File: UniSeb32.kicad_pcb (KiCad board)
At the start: 2 copper layers, 72 x 100 mm, 35 parts, among them IC1 WEMOS-D1-MINI, IC2 GY-BME280-3.3, IC3 AMS1117-3.3, IC4 MCP23008SS, IC5 RT9400, IC6 AMS5915, J1 22-27-2031-03, X61 JST-XH-05-PIN-LONG-PAD, X7 0446200002

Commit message: .
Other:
- board text added: "UniSeb32 v1.0"
- board text removed: "UniSeb8266 v1.1"

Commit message: .
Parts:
- removed @HOLE0, @HOLE1, @HOLE2, @HOLE3: , 
- removed I2C-1, I2C-2, I2C-3: MA05-1_WON, UniSeb8266:MA05-1_WON
- removed IC1: WEMOS-D1-MINI, UniSeb8266:WEMOS-D1-MINI
- removed IC2: GY-BME280-3.3, UniSeb8266:GY-BME280-3.3
- removed IC6: AMS5915, UniSeb8266:AMS5915
- removed LED1: , UniSeb8266:LED3MM
- removed R3: 390, UniSeb8266:R1206
- removed U$2: HLK-PM01, UniSeb8266:HLK-PM01
- removed the X1 at (130.8, 74.4)
- removed the X2 at (124.6, 139.1)
- removed X7: 0446200002, UniSeb8266:0446200002
- added C10: 100n, Capacitor_SMD:C_0603_1608Metric, B.Cu at (165.8, 96.8)
- added C11: 10n, Capacitor_SMD:C_0603_1608Metric, B.Cu at (179.8, 84.2)
- added C12: 2.2µ, Capacitor_SMD:C_0603_1608Metric, B.Cu at (179.8, 86.0)
- added C13: 100n, Capacitor_SMD:C_0603_1608Metric, B.Cu at (163.8, 96.8)
- added C14: 30p, Capacitor_SMD:C_0603_1608Metric, B.Cu at (171.8, 81.2)
- added C15: 30p, Capacitor_SMD:C_0603_1608Metric, B.Cu at (177.8, 81.2)
- added C3: 22µ, Capacitor_SMD:C_1206_3216Metric, B.Cu at (159.0, 97.0)
- added C4: 100n, Capacitor_SMD:C_0603_1608Metric, B.Cu at (163.5, 67.5)
- added C5: 10p, Capacitor_SMD:C_0603_1608Metric, B.Cu at (169.0, 75.9)
- added C6: 10p, Capacitor_SMD:C_0603_1608Metric, B.Cu at (166.2, 75.9)
- added C7: 10p, Capacitor_SMD:C_0603_1608Metric, B.Cu at (161.5, 67.5)
- added C8: 10p, Capacitor_SMD:C_0603_1608Metric, B.Cu at (159.5, 67.5)
- added C9: 10uf, Capacitor_SMD:C_0603_1608Metric, B.Cu at (164.5, 83.2)
- added J2: ARJM11C7-114-BA-EW2, _custom:ARJM11C7-114-BA-EW2, F.Cu at (162.6, 73.0)
- added J3: Conn_02x05_Odd_Even, Connector_PinHeader_2.54mm:PinHeader_2x05_P2.54mm_Vertical_SMD, F.Cu at (175.5, 89.5)
- added J7: Conn_01x02_Female, TerminalBlock:TerminalBlock_bornier-2_P5.08mm, F.Cu at (128.3, 74.4)
- added J8: Conn_01x02_Female, TerminalBlock:TerminalBlock_bornier-2_P5.08mm, F.Cu at (124.6, 141.7)
- added L1: L, Inductor_SMD:L_0805_2012Metric, B.Cu at (164.5, 93.8)
- added R10: 49.9 %1, Resistor_SMD:R_0603_1608Metric, B.Cu at (164.5, 92.0)
- added R11: 49.9 %1, Resistor_SMD:R_0603_1608Metric, B.Cu at (164.5, 86.8)
- added R12: 2.2k, Resistor_SMD:R_0603_1608Metric, B.Cu at (160.5, 62.0)
- added R13: 49.9 %1, Resistor_SMD:R_0603_1608Metric, B.Cu at (164.5, 88.5)
- added R14: 12.1k, Resistor_SMD:R_0603_1608Metric, B.Cu at (164.5, 85.0)
- added R15: 10k, Resistor_SMD:R_0603_1608Metric, B.Cu at (181.2, 91.2)
- added R16: 10k, Resistor_SMD:R_0603_1608Metric, B.Cu at (173.0, 122.0)
- added R17: 10k, Resistor_SMD:R_0603_1608Metric, B.Cu at (181.2, 94.8)
- added R18: 10k, Resistor_SMD:R_0603_1608Metric, B.Cu at (181.2, 93.0)
- added R19: 10k, Resistor_SMD:R_0603_1608Metric, B.Cu at (181.2, 87.8)
- added R2: 0, Resistor_SMD:R_0603_1608Metric, B.Cu at (162.5, 80.5)
- added R20: 10k, Resistor_SMD:R_0603_1608Metric, B.Cu at (181.2, 89.5)
- added R8: 2.2k, Resistor_SMD:R_0603_1608Metric, B.Cu at (162.5, 62.0)
- added R9: 49.9 %1, Resistor_SMD:R_0603_1608Metric, B.Cu at (164.5, 90.2)
- added U1: mini_esp32, ESP32_mini:ESP32_mini, F.Cu at (169.0, 114.5)
- added U2: LAN8720A, Package_DFN_QFN:QFN-24-1EP_4x4mm_P0.5mm_EP2.6x2.6mm, B.Cu at (173.0, 89.3)
- added U4: AMS5919, _custom:AMS5915, F.Cu at (156.0, 85.0)
- added U5: module_bme280, usini_sensors:module_bme280, F.Cu at (177.9, 67.2)
- added U8: HLK-PM01, Converter_ACDC:Converter_ACDC_HiLink_HLK-PMxx, F.Cu at (135.5, 83.5)
- added Y1: Crystal_GND23, Crystal:Crystal_SMD_3225-4Pin_3.2x2.5mm, B.Cu at (174.8, 81.2)
- C1: value 100µF -> 100µ; footprint UniSeb8266:E2,5-6 -> Capacitor_THT:CP_Radial_D5.0mm_P2.50mm
- C2: value 22µF -> 22µ tantalium; footprint UniSeb8266:E2,5-6 -> Capacitor_THT:CP_Radial_D5.0mm_P2.50mm
- F1: footprint UniSeb8266:TR5 -> Fuse:Fuse_Littelfuse_372_D8.50mm
- F2: value 1A T -> 550mA MT; footprint UniSeb8266:TR5 -> Fuse:Fuse_Littelfuse_372_D8.50mm
- J1: value 22-27-2031-03 -> IO; footprint UniSeb8266:6410-03 -> Connector:FanPinHeader_1x03_P2.54mm_Vertical
- J6: renamed from X61; value JST-XH-05-PIN-LONG-PAD -> SDS011; footprint UniSeb8266:JST-XH-05-PACKAGE-LONG-PAD -> Connector_JST:JST_XH_B5B-XH-A_1x05_P2.50mm_Vertical
- JP1: renamed from SJ1; value (none) -> SolderJumper_2_Open; footprint UniSeb8266:SJ -> Jumper:SolderJumper-2_P1.3mm_Open_Pad1.0x1.5mm
- JP2: renamed from SJ2; value (none) -> SolderJumper_3_Open; footprint UniSeb8266:SJ_2 -> Jumper:SolderJumper-3_P1.3mm_Open_Pad1.0x1.5mm_NumberLabels
- R1: footprint UniSeb8266:P0613V -> Resistor_THT:R_Axial_DIN0414_L11.9mm_D4.5mm_P5.08mm_Vertical
- R4, R5: footprint UniSeb8266:R1206 -> Resistor_SMD:R_0603_1608Metric
- R6, R7: value (none) -> R; footprint UniSeb8266:R1206 -> Resistor_SMD:R_0603_1608Metric
- U3: renamed from IC3; footprint UniSeb8266:SOT223 -> Package_TO_SOT_SMD:SOT-223-3_TabPin2
- U6: renamed from IC5; footprint UniSeb8266:RT9400 -> _custom:RT9400
- U7: renamed from IC4; value MCP23008SS -> MCP23008-xSS; footprint UniSeb8266:SSOP20 -> Package_SO:SSOP-20_5.3x7.2mm_P0.65mm
- X1: renamed from X8; value (none) -> 233-508; footprint UniSeb8266:233-508 -> con-wago:con-wago-233-508
- X2: renamed from X3; value (none) -> 233-503; footprint UniSeb8266:233-503 -> con-wago:con-wago-233-503
- X3: renamed from X5; value (none) -> 233-504; footprint UniSeb8266:233-504 -> con-wago:con-wago-233-504
- moved C1 46.5 mm to (129.5, 126.9), turned to -90 degrees
- moved C2 36.3 mm to (138.0, 127.0), turned to -90 degrees
- moved U6 34.4 mm to (146.0, 82.5)
- moved U3 31.4 mm to (132.0, 105.0), turned to 90 degrees
- moved R5 24.5 mm to (177.5, 122.0)
- moved R7 13.2 mm to (139.0, 103.8)
- moved F2 10.6 mm to (126.5, 118.0)
- moved R4 10.2 mm to (170.0, 122.0), turned to 90 degrees
- moved R1 5.79 mm to (134.5, 123.0), turned to 90 degrees
- moved J6 5.21 mm to (160.0, 129.5), turned to 0 degrees
- moved F1 3.36 mm to (119.0, 68.5)
- moved J1 2.86 mm to (176.0, 139.0), turned to 0 degrees
- moved R6 1.73 mm to (139.0, 108.5), turned to 90 degrees
- turned U7 to 180 degrees
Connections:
- net COUNTER renamed /COUNTER
- net ONEWIRE renamed /ONEWIRE
- J1 pad 2: D5 -> /IO33
- J1 pad 3: D0 -> /IO32
- J6 pad 1: (no net) -> /SDS_TX
- J6 pad 2: +5V -> /SDS_RX
- J6 pad 4: SDS_RX -> +5V
- J6 pad 5: SDS_TX -> unconnected-(J6-Pad5)
- JP1 pad 1: VCC -> +5V
- JP1 pad 2: +5V -> VCC
- JP2 pad 1: N$7 -> Net-(JP2-Pad1)
- R1 pad 1: VCC -> GND
- R1 pad 2: GND -> VCC
- R4 pad 2: +3V3 -> +3.3V
- R5 pad 2: +3V3 -> +3.3V
- R6 pad 2: N$21 -> Net-(R7-Pad1)
- R7 pad 1: N$7 -> Net-(R7-Pad1)
- R7 pad 2: N$21 -> Net-(JP2-Pad1)
- U3 pad 2: +3V3 -> +3.3V
- U6 pad P$1: N$18 -> /VA1
- U6 pad P$2: N$17 -> /VA2
- U6 pad P$3: N$16 -> /VB1
- U6 pad P$4: N$4 -> /VB2
- U6 pad P$6: N$7 -> Net-(JP2-Pad1)
- U6 pad P$7: N$21 -> Net-(R7-Pad1)
- U7 pad 1: SCL -> /SCL
- U7 pad 10: (no net) -> unconnected-(U7-Pad10)
- U7 pad 11: (no net) -> unconnected-(U7-Pad11)
- U7 pad 2: SDA -> /SDA
- U7 pad 20: +3V3 -> +3.3V
- U7 pad 6: +3V3 -> +3.3V
- U7 pad 7: (no net) -> unconnected-(U7-Pad7)
- U7 pad 8: EXP-INT -> unconnected-(U7-Pad8)
- X1 pad A1: (no net) -> unconnected-(X1-PadA1)
- X1 pad A2: (no net) -> unconnected-(X1-PadA2)
- X1 pad A3: (no net) -> unconnected-(X1-PadA3)
- X1 pad A4: (no net) -> unconnected-(X1-PadA4)
- X1 pad A5: (no net) -> unconnected-(X1-PadA5)
- X1 pad A6: (no net) -> unconnected-(X1-PadA6)
- X1 pad A7: (no net) -> unconnected-(X1-PadA7)
- X1 pad A8: (no net) -> unconnected-(X1-PadA8)
- X2 pad A1: (no net) -> unconnected-(X2-PadA1)
- X2 pad A2: (no net) -> unconnected-(X2-PadA2)
- X2 pad A3: (no net) -> unconnected-(X2-PadA3)
- X2 pad B3: +3V3 -> +3.3V
- X3 pad A1: (no net) -> unconnected-(X3-PadA1)
- X3 pad A2: (no net) -> unconnected-(X3-PadA2)
- X3 pad A3: (no net) -> unconnected-(X3-PadA3)
- X3 pad A4: (no net) -> unconnected-(X3-PadA4)
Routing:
- net +3V3: track 165.3 -> 0.00 mm, vias 2 -> 0
- net SCL: track 127.1 -> 0.00 mm, vias 1 -> 0
- net +5V: track 222.2 -> 112.4 mm, vias 3 -> 1
- net SDA: track 109.3 -> 0.00 mm, vias 1 -> 0
- net +3.3V: track 0.00 -> 60.5 mm, vias 0 -> 1
- net /COUNTER: track 55.4 -> 0.00 mm, vias 2 -> 0
- net N$7: track 48.9 -> 0.00 mm, vias 1 -> 0
- net D0: track 46.2 -> 0.00 mm, vias 3 -> 0
- net D5: track 43.9 -> 0.00 mm, vias 2 -> 0
- net N$18: track 38.4 -> 0.00 mm
- net SDS_TX: track 34.9 -> 0.00 mm
- net N$4: track 34.2 -> 0.00 mm
- net VCC: track 34.0 -> 0.00 mm, vias 1 -> 0
- net /ONEWIRE: track 57.2 -> 25.2 mm, vias 2 -> 1
- net /VA1: track 0.00 -> 31.6 mm
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
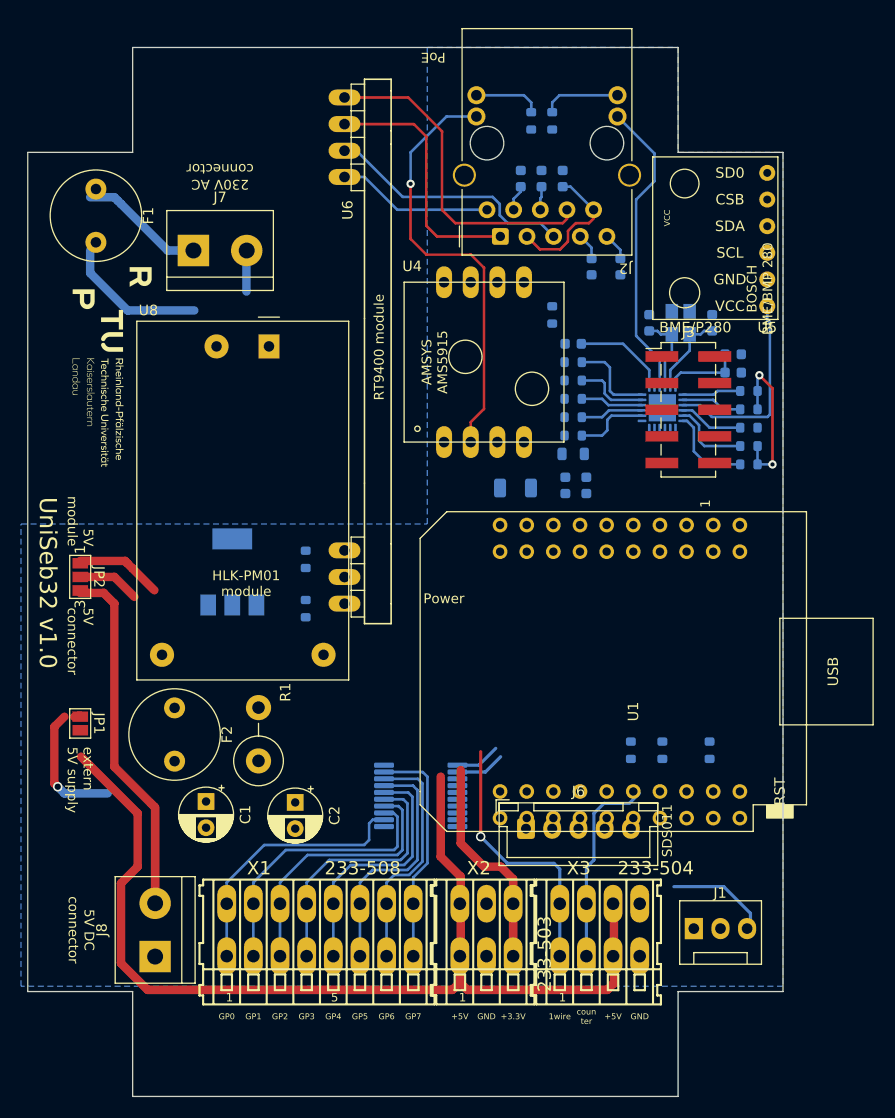
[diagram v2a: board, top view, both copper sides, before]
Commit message: switched to 4 layer PCB. Routed remaining airwires
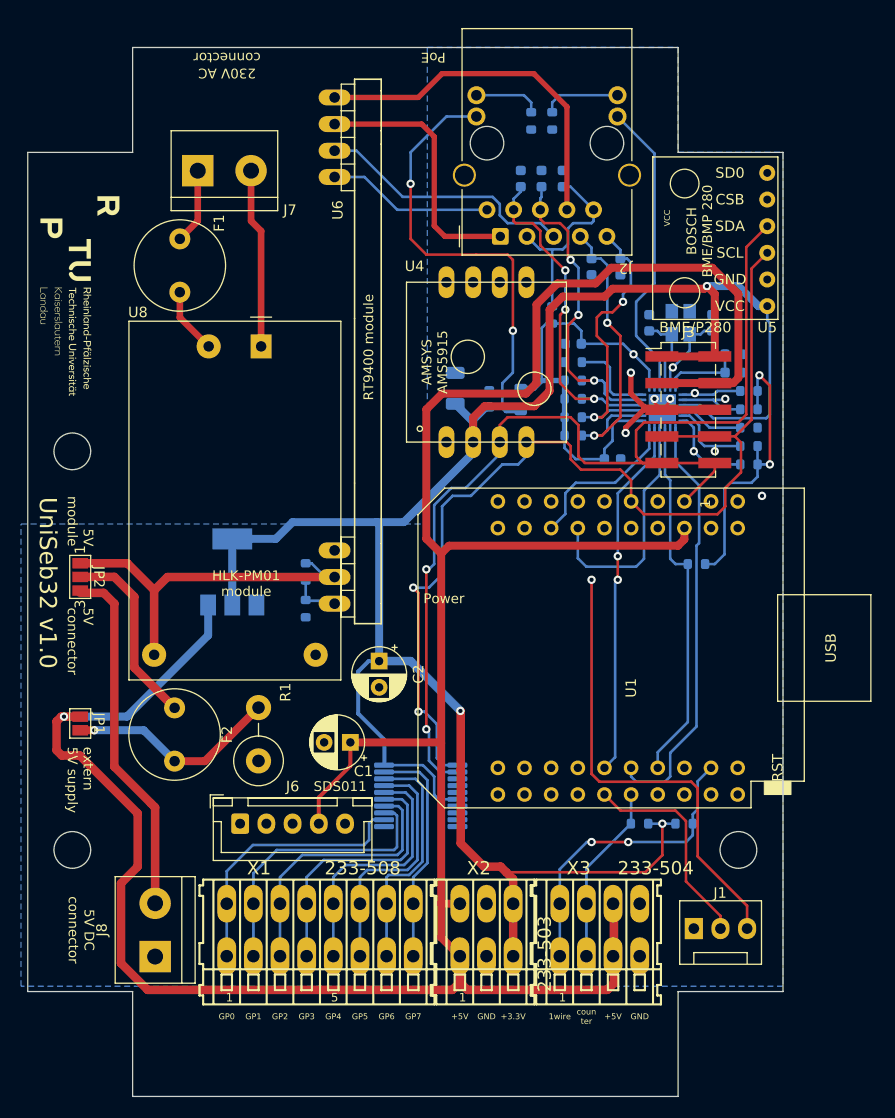
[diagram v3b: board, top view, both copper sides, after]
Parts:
- added REF**: MountingHole_3.5mm, MountingHole:MountingHole_3.5mm, F.Cu at (180.3, 131.5)
- added REF**: MountingHole_3.5mm, MountingHole:MountingHole_3.5mm, F.Cu at (116.8, 131.5)
- added REF**: MountingHole_3.5mm, MountingHole:MountingHole_3.5mm, F.Cu at (116.8, 93.5)
- moved J6 27.3 mm to (132.8, 129.0)
- moved R16 18.0 mm to (176.2, 104.2), turned to 0 degrees
- moved C2 15.7 mm to (146.0, 113.5)
- moved C1 14.9 mm to (143.3, 121.2), turned to 180 degrees
- moved C3 11.1 mm to (153.2, 87.5), turned to 90 degrees
- moved C13 11.0 mm to (156.5, 88.5), turned to 90 degrees
- moved F1 9.30 mm to (127.0, 73.2)
- moved J7 7.62 mm to (128.7, 66.8)
- moved R5 7.41 mm to (175.1, 129.0), turned to 180 degrees
- moved L1 7.20 mm to (159.5, 88.6), turned to 90 degrees
- moved R4 7.05 mm to (170.8, 129.0), turned to 0 degrees
- moved C10 3.54 mm to (168.2, 94.2), turned to 0 degrees
- moved U1 2.26 mm to (168.8, 112.2)
- moved R7 1.20 mm to (139.0, 105.0)
- moved U6 0.95 mm to (145.1, 82.5)
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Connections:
- net /EMAC_MDIO renamed /EMAC_MDI0
- U1 pad 10: /EMAC_TXDO -> /EMAC_TXD0
- X1 pad A1: unconnected-(X1-PadA1) -> Net-(U7-Pad12)
- X1 pad A2: unconnected-(X1-PadA2) -> Net-(U7-Pad13)
- X1 pad A3: unconnected-(X1-PadA3) -> Net-(U7-Pad14)
- X1 pad A4: unconnected-(X1-PadA4) -> Net-(U7-Pad15)
- X1 pad A5: unconnected-(X1-PadA5) -> Net-(U7-Pad16)
- X1 pad A6: unconnected-(X1-PadA6) -> Net-(U7-Pad17)
- X1 pad A7: unconnected-(X1-PadA7) -> Net-(U7-Pad18)
- X1 pad A8: unconnected-(X1-PadA8) -> Net-(U7-Pad19)
- X2 pad A1: unconnected-(X2-PadA1) -> +5V
- X2 pad A2: unconnected-(X2-PadA2) -> GND
- X2 pad A3: unconnected-(X2-PadA3) -> +3.3V
- X3 pad A1: unconnected-(X3-PadA1) -> /ONEWIRE
- X3 pad A2: unconnected-(X3-PadA2) -> /COUNTER
- X3 pad A3: unconnected-(X3-PadA3) -> +5V
- X3 pad A4: unconnected-(X3-PadA4) -> GND
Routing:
- net +3.3V: track 60.5 -> 249.0 mm, vias 1 -> 5
- net +5V: track 112.4 -> 263.4 mm
- net /SDA: track 4.60 -> 103.5 mm, vias 0 -> 2
- net /SCL: track 4.19 -> 98.2 mm, vias 0 -> 2
- net 3V3-2: track 24.7 -> 82.7 mm, vias 2 -> 3
- net /SDS_TX: track 0.00 -> 54.6 mm
- net /EMAC_RXD1: track 5.63 -> 59.0 mm, vias 0 -> 1
- net /IO32: track 9.94 -> 52.5 mm, vias 0 -> 1
- net /SDS_RX: track 0.00 -> 41.6 mm
- net /EMAC_MDI0: track 8.52 -> 49.7 mm, vias 0 -> 1
- net /EMAC_MDC: track 0.00 -> 40.3 mm
- net GND: track 0.00 -> 36.4 mm, vias 0 -> 5
- net /IO5_RST: track 0.00 -> 35.2 mm
- net /EMAC_TXD0: track 0.00 -> 34.4 mm, vias 0 -> 2
- net /EMAC_RXD0: track 5.86 -> 37.2 mm, vias 0 -> 1
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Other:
- copper layers 2 -> 4
